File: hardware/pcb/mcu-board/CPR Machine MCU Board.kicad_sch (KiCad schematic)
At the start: 0 parts

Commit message: Started initial layout for mcu board
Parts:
- added C3, C4, C5, C6, C7, C8: 100n, symbol Device:C
- added C9: 4.7u, symbol Device:C
- added U1: STM32G441VBTx, Package_QFP:LQFP-100_14x14mm_P0.5mm, symbol MCU_ST_STM32G4:STM32G441VBTx
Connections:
- new net +3.3V: C3.1, C4.1, C5.1, C6.1, C7.1, C8.1, C9.1
- new net GND: C3.2, C4.2, C5.2, C6.2, C7.2, C8.2, C9.2, U1.23 (VSS), U1.35 (VSSA), U1.48 (VSS), U1.63 (VSS), U1.74 (VSS), U1.99 (VSS)
- new net decoupling_bus: U1.100 (VDD), U1.24 (VDD), U1.49 (VDD), U1.6 (VBAT), U1.64 (VDD), U1.75 (VDD)

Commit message: Small fix
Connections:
- net decoupling_bus is gone; now on net +3.3V: U1.100 (VDD), U1.24 (VDD), U1.49 (VDD), U1.6 (VBAT), U1.64 (VDD), U1.75 (VDD)
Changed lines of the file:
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@@
 		(color 0 0 0 0)
-	)
-	(bus_entry
-		(at 261.62 78.74)
-		(size 2.54 2.54)
-		(stroke
-			(width 0)
-			(type default)
-		)
 	)
 	(wire
@@
 		)
 		(stroke
+			(width 0)
+			(type default)
+		)
+	)
+	(wire
+		(pts
+			(xy 88.9 24.13) (xy 99.06 24.13)
+		)
+		(stroke

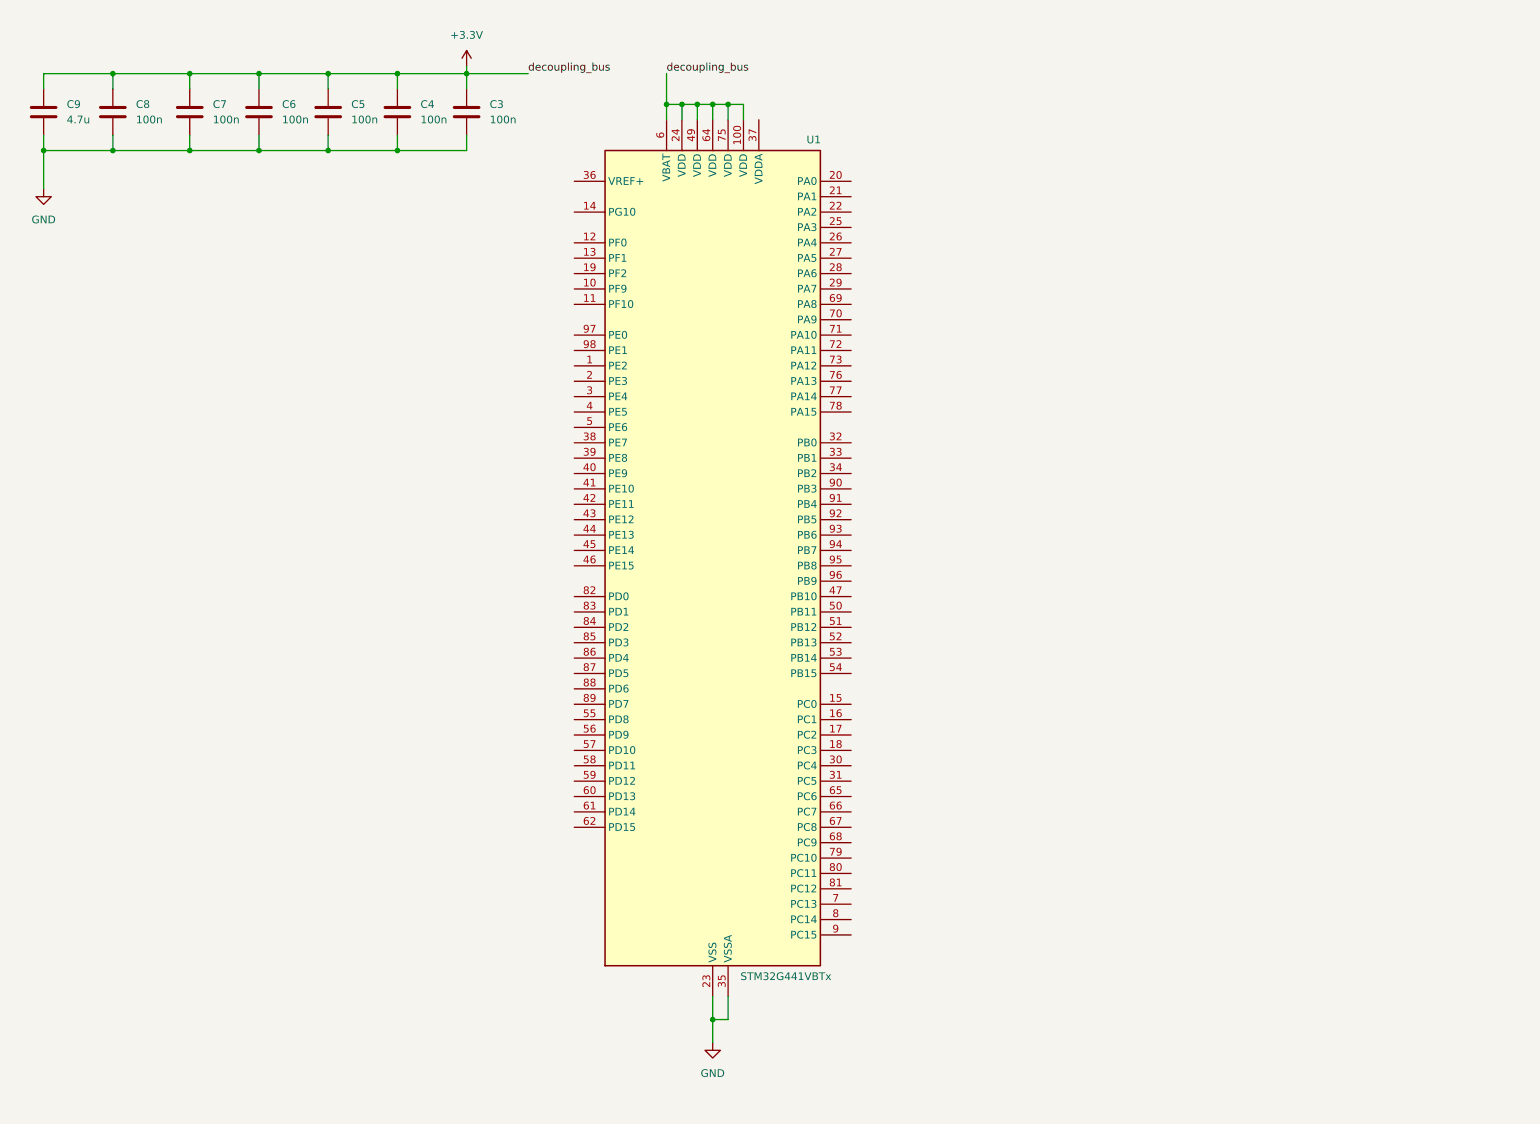
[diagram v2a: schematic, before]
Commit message: Added decoupling, added VDDA filtering, labels for potential crytal oscilator
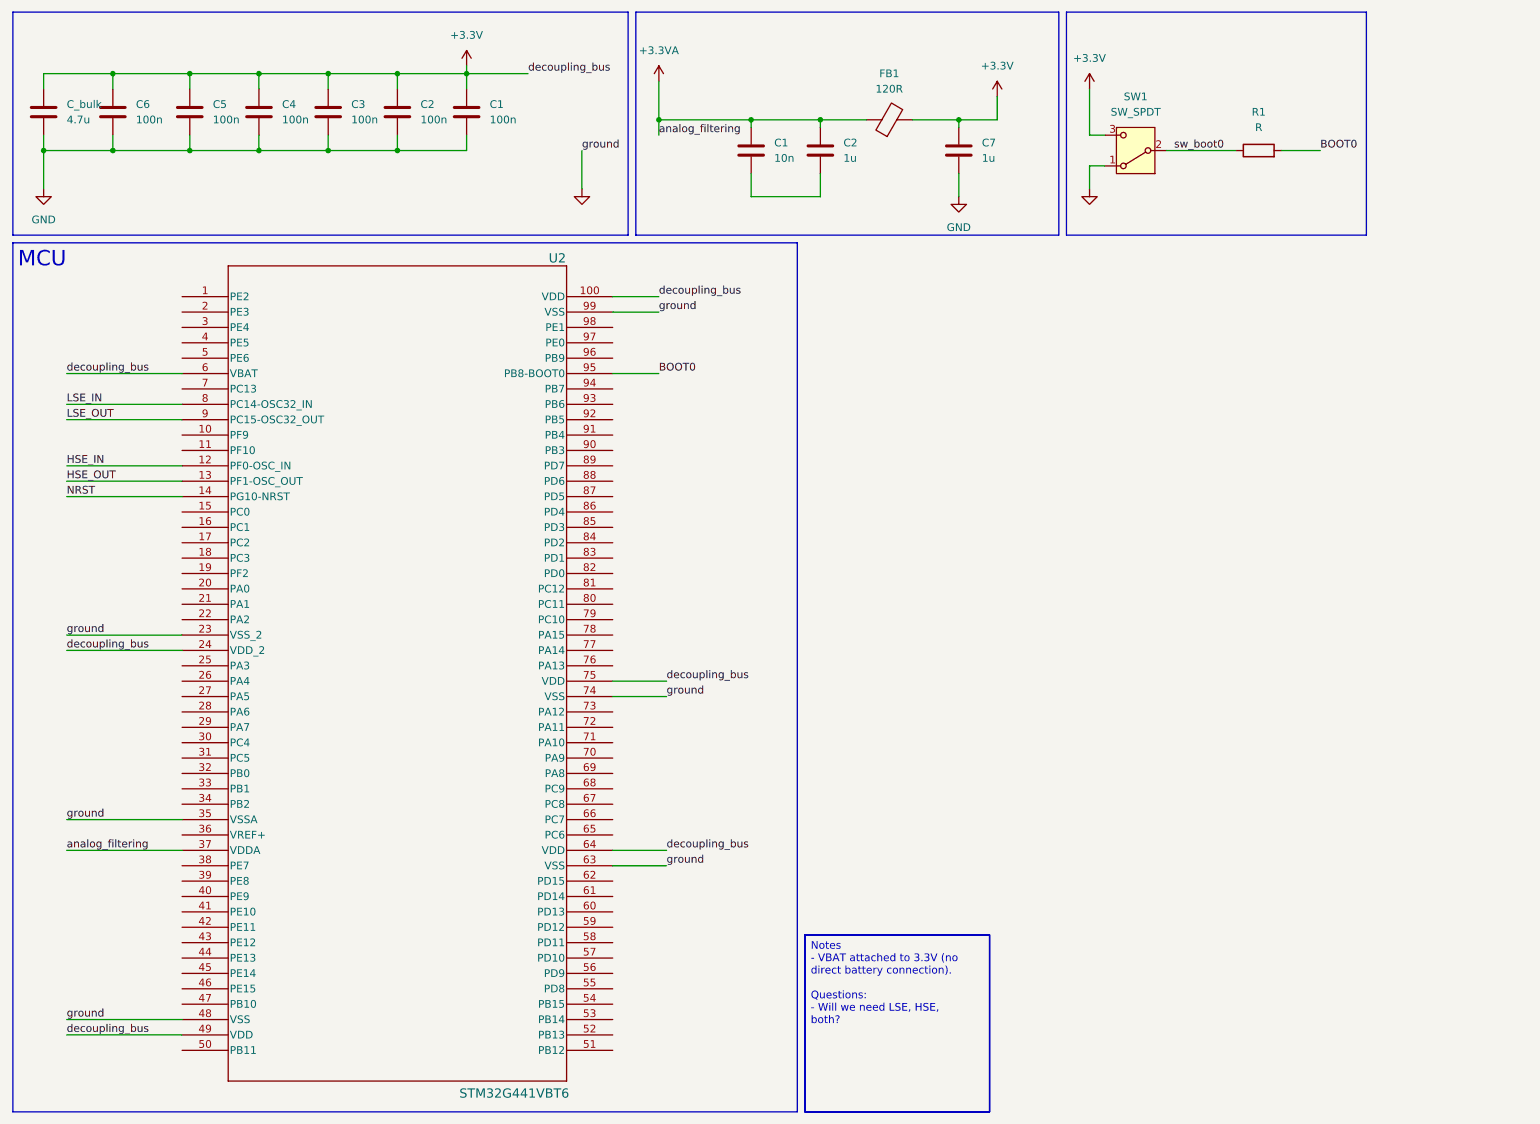
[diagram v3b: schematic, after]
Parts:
- removed U1: STM32G441VBTx, Package_QFP:LQFP-100_14x14mm_P0.5mm, symbol MCU_ST_STM32G4:STM32G441VBTx
- added C1: 10n, symbol Device:C
- added C2, C7: 1u, symbol Device:C
- added FB1: 120R, symbol Device:FerriteBead
- added R1: R, symbol Device:R
- added SW1: SW_SPDT, symbol Switch:SW_SPDT
- added U2: STM32G441VBT6, LQFP100-14x14mm_STM, symbol STM32G441VBT6_symb:STM32G441VBT6
- renumbered C3 to C1, C4 to C2, C5 to C3, C6 to C4, C7 to C5, C8 to C6, C9 to C_bulk
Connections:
- net +3.3V: now also C7.1, FB1.2, SW1.3 (C), U2.100 (VDD), U2.24 (VDD_2), U2.49 (VDD), U2.6 (VBAT), U2.64 (VDD), U2.75 (VDD)
- net GND: now also C7.2
- new net: C1.2, C2.2
- new net +3.3VA: C1.1, C2.1, FB1.1, U2.37 (VDDA)
- new net BOOT0: R1.2, U2.95 (PB8-BOOT0)
- new net HSE_IN: U2.12 (PF0-OSC_IN)
- new net HSE_OUT: U2.13 (PF1-OSC_OUT)
- new net LSE_IN: U2.8 (PC14-OSC32_IN)
- new net LSE_OUT: U2.9 (PC15-OSC32_OUT)
- new net NRST: U2.14 (PG10-NRST)
- new net ground: U2.23 (VSS_2), U2.35 (VSSA), U2.48 (VSS), U2.63 (VSS), U2.74 (VSS), U2.99 (VSS)
- new net sw_boot0: R1.1, SW1.2 (B)
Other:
- note added: "MCU"
